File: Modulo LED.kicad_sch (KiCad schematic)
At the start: 4 parts, among them J1 Conn_01x02_Pin

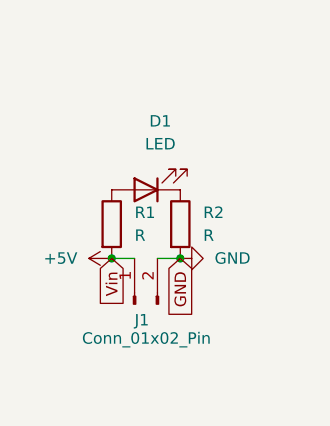
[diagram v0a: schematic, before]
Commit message: Added filters and overvoltage protecion circuit
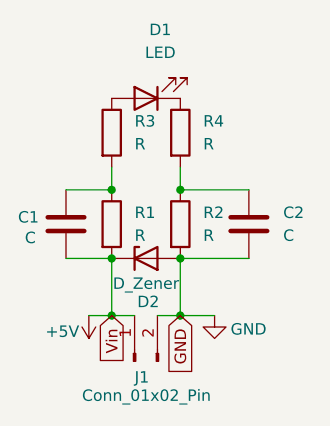
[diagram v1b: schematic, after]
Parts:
- added C1, C2: C, Capacitor_SMD:C_0603_1608Metric, symbol Device:C
- added D2: D_Zener, Diode_SMD:D_0603_1608Metric, symbol Device:D_Zener
- added R3, R4: R, Resistor_SMD:R_0201_0603Metric, symbol Device:R
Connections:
- net +5V: now also C1.2, D2.1 (K)
- net GND: now also C2.2, D2.2 (A)
- net at R1.1: now also C1.1, R3.2; no longer D1.2 (A)
- net at R2.1: now also C2.1, R4.2; no longer D1.1 (K)
- new net: D1.2 (A), R3.1
- new net: D1.1 (K), R4.1
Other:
- moved on the sheet: D1, J1
